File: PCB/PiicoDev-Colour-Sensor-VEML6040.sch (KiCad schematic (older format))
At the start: 19 parts, among them J1 , J2 , J3 Conn_PiicoDev_header_01x04_Ma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, U1 VEML6040

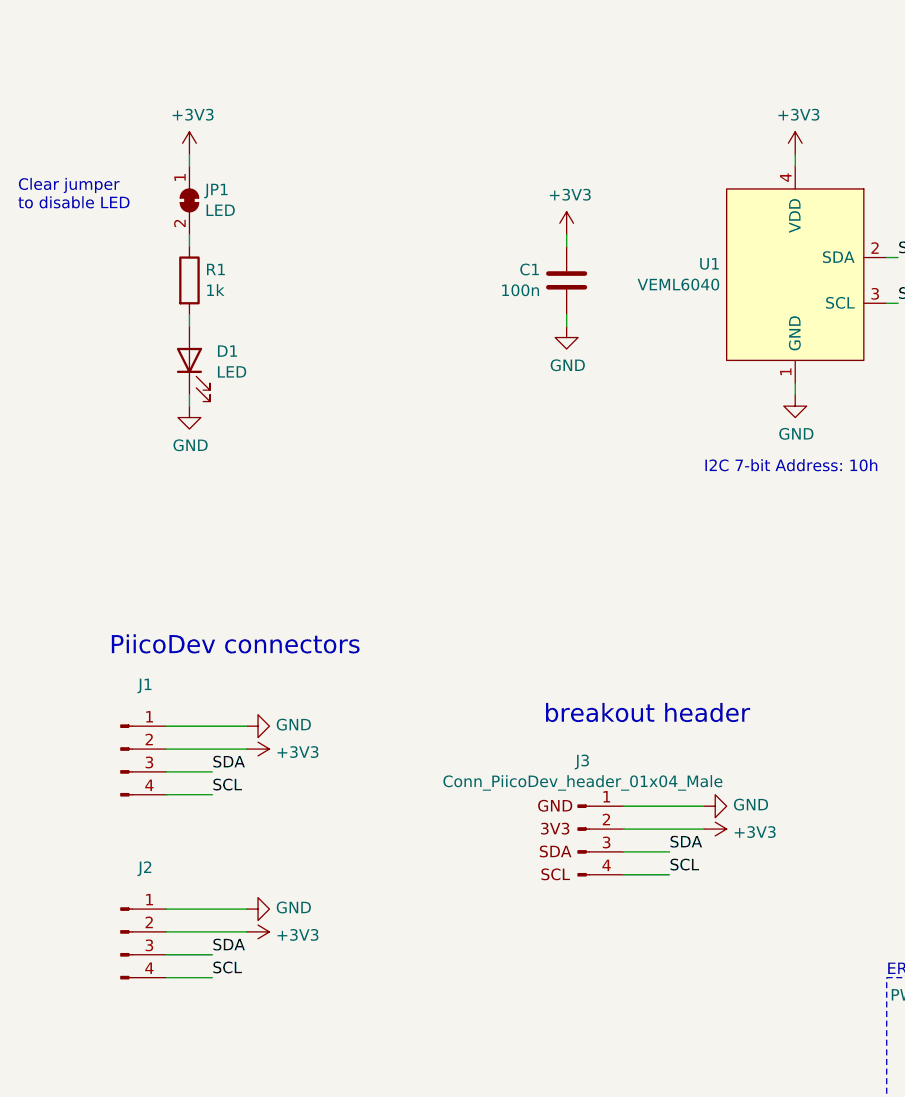
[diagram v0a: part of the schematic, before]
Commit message: Replace power LED with illumination LED
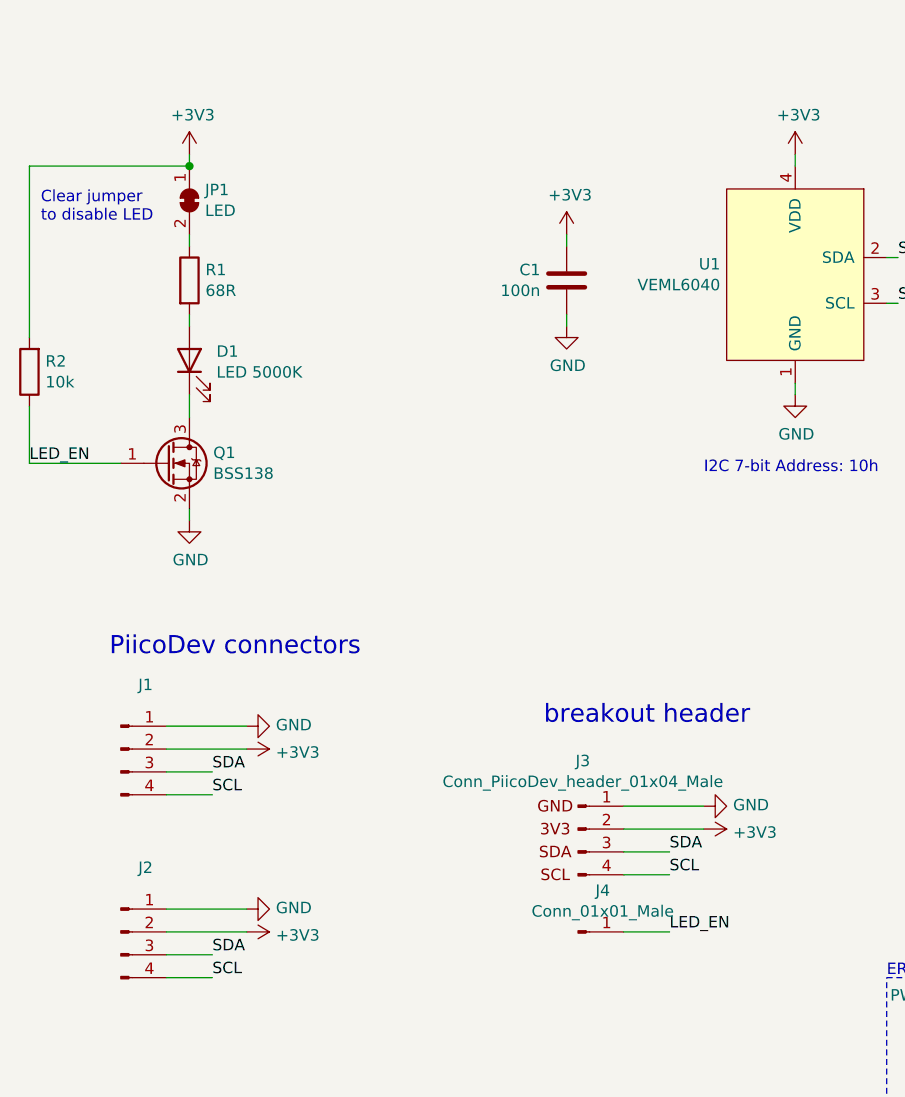
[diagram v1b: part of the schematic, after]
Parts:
- added J4: Conn_01x01_Male, CoreElectronics_Components:PiicoDev_header_1pin_LED, symbol Connector:Conn_01x01_Male
- added Q1: BSS138, Package_TO_SOT_SMD:SOT-23, symbol Transistor_FET:BSS138
- added R2: 10k, Resistor_SMD:R_0402_1005Metric, symbol Device:R
- D1: value LED -> LED 5000K; footprint LED_SMD:LED_0603_1608Metric -> CoreElectronics_Components:LED_1208_3020Metric_Heatsink
- R1: value 1k -> 68R
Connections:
- net +3V3: now also R2.2
- net GND: now also Q1.2 (S); no longer D1.1 (K)
- new net: D1.1 (K), Q1.3 (D)
- new net LED_EN: J4.1 (Pin_1), Q1.1 (G), R2.1
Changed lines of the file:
@@
 P 2200 4100
 F 0 "D1" V 2239 3982 50  0000 R CNN
-F 1 "LED" V 2148 3982 50  0000 R CNN
-F 2 "LED_SMD:LED_0603_1608Metric" H 2200 4100 50  0001 C CNN
+F 1 "LED 5000K" V 2148 3982 50  0000 R CNN
+F 2 "CoreElectronics_Components:LED_1208_3020Metric_Heatsink" H 2200 4100 50  0001 C CNN
 F 3 "~" H 2200 4100 50  0001 C CNN
 	1    2200 4100
@@
 L power:GND #PWR0105
 U 1 1 5F914478
-P 2200 4300
-F 0 "#PWR0105" H 2200 4050 50  0001 C CNN
-F 1 "GND" H 2205 4127 50  0000 C CNN
-F 2 "" H 2200 4300 50  0001 C CNN
-F 3 "" H 2200 4300 50  0001 C CNN
-	1    2200 4300
-	1    0    0    -1
-$EndComp
-Wire Wire Line
-	2200 4300 2200 4250
+P 2200 4800
+F 0 "#PWR0105" H 2200 4550 50  0001 C CNN
+F 1 "GND" H 2205 4627 50  0000 C CNN
+F 2 "" H 2200 4800 50  0001 C CNN
+F 3 "" H 2200 4800 50  0001 C CNN
+	1    2200 4800
+	1    0    0    -1
+$EndComp
 $Comp
 L power:+3V3 #PWR0106
@@
 P 2200 3750
 F 0 "R1" H 2270 3796 50  0000 L CNN
-F 1 "1k" H 2270 3705 50  0000 L CNN
+F 1 "68R" H 2270 3705 50  0000 L CNN
 F 2 "Resistor_SMD:R_0402_1005Metric" V 2130 3750 50  0001 C CNN
 F 3 "~" H 2200 3750 50  0001 C CNN
@@
 Wire Wire Line
 	2200 3950 2200 3900
-Text Notes 1450 3450 0    50   ~ 0
-Clear jumper \nto disable LED
 Text Notes 2100 1100 0    50   ~ 0
 Clear jumper \nto remove I2C pullup
@@
 Wire Wire Line
 	5250 3650 5300 3650
+$Comp
+L Transistor_FET:BSS138 Q1
+U 1 1 6098B4D7
+P 2100 4550
+F 0 "Q1" H 2304 4596 50  0000 L CNN
+F 1 "BSS138" H 2304 4505 50  0000 L CNN
+F 2 "Package_TO_SOT_SMD:SOT-23" H 2300 4475 50  0001 L CIN
+F 3 "https://www.onsemi.com/pub/Collateral/BSS138-D.PDF" H 2100 4550 50  0001 L CNN
+	1    2100 4550
+	1    0    0    -1
+$EndComp
+Wire Wire Line
+	2200 4250 2200 4350
+Wire Wire Line
+	2200 4750 2200 4800
+$Comp
+L Connector:Conn_01x01_Male J4
+U 1 1 609966CF
+P 3900 6600
+F 0 "J4" H 4008 6781 50  0000 C CNN
+F 1 "Conn_01x01_Male" H 4008 6690 50  0000 C CNN
+F 2 "CoreElectronics_Components:PiicoDev_header_1pin_LED" H 3900 6600 50  0001 C CNN
+F 3 "~" H 3900 6600 50  0001 C CNN
+	1    3900 6600
+	1    0    0    -1
+$EndComp
+Connection ~ 2200 3250
+Text Notes 1550 3500 0    50   ~ 0
+Clear jumper \nto disable LED
+$Comp
+L Device:R R2
+U 1 1 6098F966
+P 1500 4150
+F 0 "R2" H 1430 4104 50  0000 R CNN
+F 1 "10k" H 1430 4195 50  0000 R CNN
+F 2 "Resistor_SMD:R_0402_1005Metric" V 1430 4150 50  0001 C CNN
+F 3 "~" H 1500 4150 50  0001 C CNN
+	1    1500 4150
+	-1   0    0    1
+$EndComp
+Wire Wire Line
+	1900 4550 1500 4550
+Wire Wire Line
+	1500 4550 1500 4300
+Wire Wire Line
+	1500 4000 1500 3250
+Wire Wire Line
+	1500 3250 2200 3250
+Text Label 1500 4550 0    50   ~ 0
+LED_EN
+Wire Wire Line
+	4100 6600 4300 6600
+Text Label 4300 6600 0    50   ~ 0
+LED_EN
 $EndSCHEMATC
